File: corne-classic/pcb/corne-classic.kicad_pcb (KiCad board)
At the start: 2 copper layers, 133.8 x 92.2 mm, 98 parts, among them J3 LED, P1 i2c-pin, P2 i2c-pin, SW1 SW_PUSH, SW10 SW_PUSH, SW11 SW_PUSH, SW12 SW_PUSH, SW13 SW_PUSH, SW14 SW_PUSH, SW15 SW_PUSH, SW16 SW_PUSH, SW17 SW_PUSH, SW18 SW_PUSH, SW19 SW_PUSH, SW2 SW_PUSH, SW20 SW_PUSH, SW21 SW_PUSH, SW3 SW_PUSH, SW4 SW_PUSH, SW5 SW_PUSH, SW6 SW_PUSH, SW7 SW_PUSH, SW8 SW_PUSH, SW9 SW_PUSH, U1 ProMicro

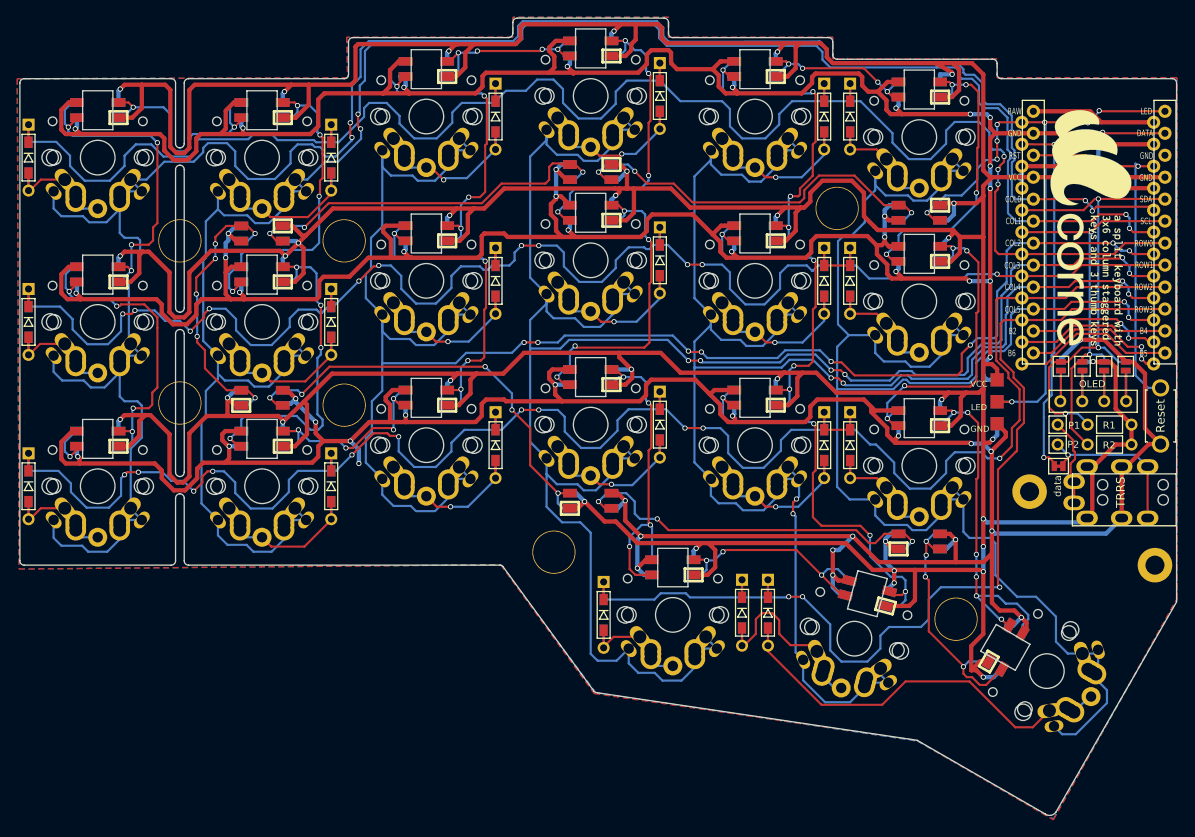
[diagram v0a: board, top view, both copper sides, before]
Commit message: Update LED foot prints
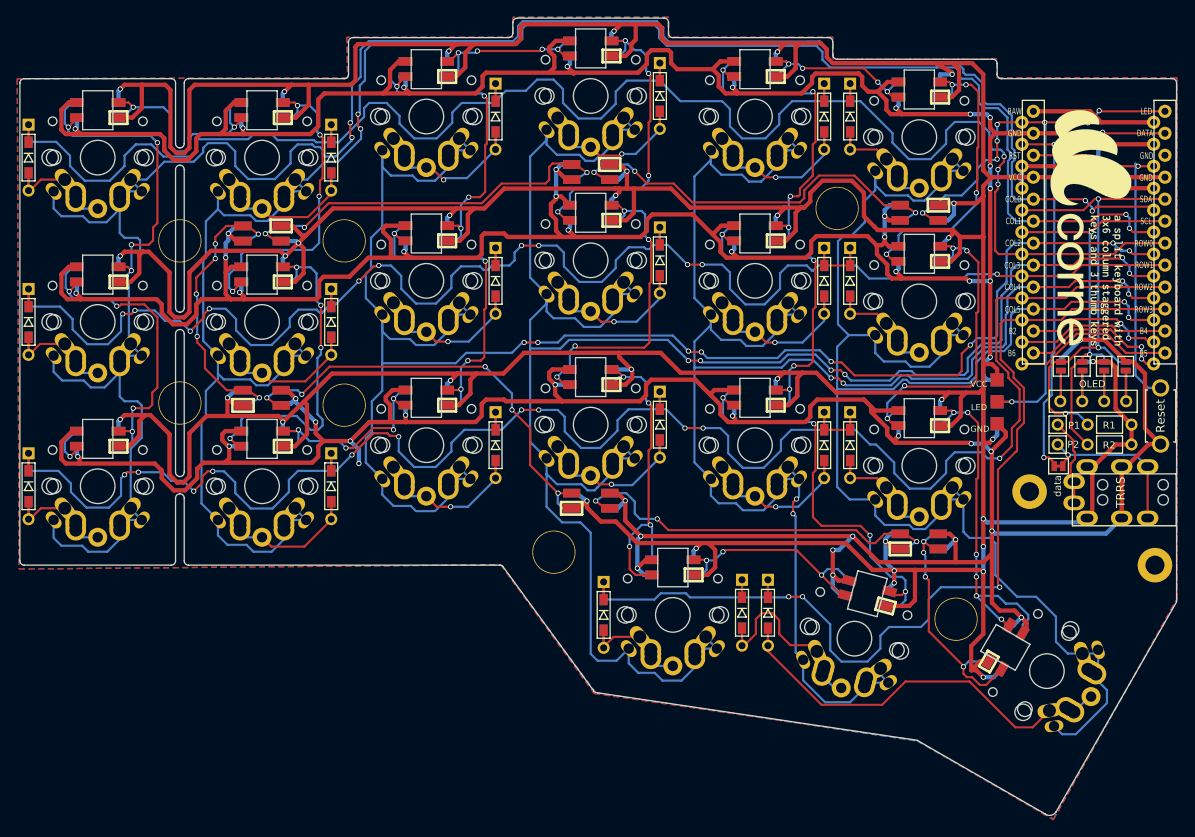
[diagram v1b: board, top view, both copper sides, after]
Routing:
- net Net-(L23-Pad3): track 46.4 -> 48.0 mm
- net Net-(L22-Pad3): track 45.1 -> 46.7 mm
- net Net-(L22-Pad1): track 33.1 -> 34.5 mm
- net Net-(L26-Pad1): track 44.5 -> 45.8 mm
- net LED: track 76.9 -> 77.7 mm
- net col1: track 222.0 -> 221.3 mm
- net VCC: track 758.2 -> 758.8 mm
- net Net-(L25-Pad1): track 51.6 -> 52.1 mm
